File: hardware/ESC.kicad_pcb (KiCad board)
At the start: 2 copper layers, 60 x 25 mm, 83 parts, among them J1 +, J2 -, J3 Conn_01x03, J4 +, J5 +, J6 +, J7 Conn_01x03, Q1 AGM60P30AP, Q2 AGM60P30AP, Q3 AGM60P30AP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

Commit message: layout first draft
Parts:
- C10, C11, C12, C13, C7, C9, D2, FB1, R10, R13, R14, R15: moved to B.Cu
- C14: footprint Capacitor_SMD:C_0402_1005Metric -> Capacitor_SMD:C_0603_1608Metric; moved to B.Cu
- C22, C23: footprint Capacitor_SMD:C_0603_1608Metric -> Capacitor_SMD:C_0402_1005Metric
- C29, C8: footprint Capacitor_SMD:C_0402_1005Metric -> Capacitor_SMD:C_0603_1608Metric
- Q7: value NCE55P30K -> AGM60P30A; footprint Package_TO_SOT_SMD:TO-252-2 -> Package_DFN_QFN:PQFN-8-EP_6x5mm_P1.27mm_Generic; moved to B.Cu
- moved C6 83.0 mm to (180.3, 104.9), turned to 90 degrees
- moved C2 82.8 mm to (180.3, 88.7), turned to 90 degrees
- moved C4 82.8 mm to (180.3, 96.6), turned to 90 degrees
- moved C5 79.3 mm to (176.0, 108.2), turned to -90 degrees
- moved C3 78.8 mm to (176.0, 99.9), turned to -90 degrees
- moved C1 78.6 mm to (176.0, 92.0), turned to -90 degrees
- moved C25 76.2 mm to (178.7, 107.1), turned to 90 degrees
- moved C17 76.1 mm to (178.4, 104.4), turned to 180 degrees
- moved C22 75.4 mm to (178.8, 98.8), turned to 90 degrees
- moved C16 75.4 mm to (178.4, 96.1), turned to 180 degrees
- moved C15 75.2 mm to (178.4, 88.2), turned to 180 degrees
- moved R9 73.9 mm to (181.5, 105.5), turned to 90 degrees
- moved R2 73.6 mm to (181.5, 89.3), turned to 90 degrees
- moved R6 72.9 mm to (181.5, 97.2), turned to 90 degrees
- moved R16 72.7 mm to (181.3, 99.2), turned to 180 degrees
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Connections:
- C3 pad 2: /MOTOR_A -> /MOTOR_B
- C5 pad 2: /MOTOR_A -> /MOTOR_C
- J5 pad 1: /MOTOR_A -> /MOTOR_B
- J6 pad 1: /MOTOR_A -> /MOTOR_C
- Q3 pad 1: /MOTOR_A -> /MOTOR_B
- Q3 pad 2: /GHA -> /GHB
- Q4 pad 2: /GLA -> /GLB
- Q4 pad 3: /MOTOR_A -> /MOTOR_B
- Q5 pad 1: /MOTOR_A -> /MOTOR_C
- Q5 pad 2: /GHA -> /GHC
- Q6 pad 2: /GLA -> /GLC
- Q6 pad 3: /MOTOR_A -> /MOTOR_C
- Q7 pad 1: (no net) -> VBUS
- Q7 pad 2: (no net) -> Net-(Q7-G)
- Q7 pad 3: (no net) -> Net-(D2-A2)
- R13 pad 1: Net-(Q7-PadG) -> Net-(Q7-G)
- R16 pad 1: /MOTOR_A -> /MOTOR_B
- R22 pad 1: /MOTOR_A -> /MOTOR_C
- R6 pad 1: /MOTOR_A -> /MOTOR_B
- R9 pad 1: /MOTOR_A -> /MOTOR_C
- U1 pad 16: /SHB -> /MOTOR_B
- U1 pad 19: /SHC -> /MOTOR_C
- U1 pad 49: unconnected-(U1-EP-Pad49) -> GND
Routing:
- net GND: track 0.00 -> 23.5 mm, vias 0 -> 50
- net /BGND: track 0.00 -> 5.17 mm
- net Net-(U1-CB): track 0.00 -> 1.32 mm
- net VBUS: track 0.00 -> 1.24 mm, vias 0 -> 100
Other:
- copper layers 2 -> 4

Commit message: started routing schematic
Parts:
- added J8: +, Connector_Wire:SolderWirePad_1x01_SMD_2x4mm, B.Cu at (151.6, 107.0)
- added J9: +, Connector_Wire:SolderWirePad_1x01_SMD_2x4mm, B.Cu at (155.1, 107.0)
- J3: value Conn_01x03 -> +; footprint Connector_PinHeader_2.54mm:PinHeader_1x03_P2.54mm_Vertical -> Connector_Wire:SolderWirePad_1x01_SMD_2x4mm; moved to B.Cu
- moved J3 8.47 mm to (148.0, 107.0), turned to 0 degrees
- moved J1 8.00 mm to (142.0, 89.0)
- moved J2 8.00 mm to (142.0, 106.0)
- moved J7 8.00 mm to (140.0, 95.0)
- moved JP1 7.95 mm to (143.1, 98.2)
- moved R20 7.95 mm to (143.3, 100.3)
- moved D2 7.30 mm to (148.6, 88.1)
- moved Q7 7.20 mm to (148.8, 92.8)
- moved R13 7.20 mm to (150.9, 96.5)
- moved C32 7.20 mm to (146.4, 94.2)
- moved R24 7.20 mm to (148.4, 94.2)
- moved R25 7.20 mm to (147.4, 94.2)
- moved C18 7.15 mm to (166.2, 89.7)
- moved C19 7.15 mm to (158.2, 89.6)
- moved C20 7.15 mm to (150.0, 89.6)
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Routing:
- net /MOTOR_A: track 0.00 -> 55.4 mm, vias 0 -> 1
- net /SPA: track 0.00 -> 42.3 mm, vias 0 -> 2
- net /GLA: track 0.00 -> 38.2 mm, vias 0 -> 2
- net VBUS: track 1.24 -> 26.4 mm, vias 100 -> 64
- net /GHA: track 0.00 -> 22.3 mm, vias 0 -> 2
- net /MOTOR_C: track 0.00 -> 12.5 mm
- net /MOTOR_B: track 0.00 -> 12.5 mm
- net /VIRTUAL_N: track 0.00 -> 9.69 mm
- net /SPC: track 0.00 -> 8.08 mm, vias 0 -> 1
- net /SPB: track 0.00 -> 7.92 mm, vias 0 -> 1
- net /HSE_IN: track 0.00 -> 6.72 mm
- net /BEMF_C: track 0.00 -> 5.02 mm
- net +3.3V: track 0.00 -> 4.88 mm
- net /BEMF_B: track 0.00 -> 4.81 mm
- net /BEMF_A: track 0.00 -> 4.59 mm
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- added copper zone on B.Cu, net /MOTOR_A
- added copper zone on B.Cu, net /MOTOR_B
- added copper zone on B.Cu, net /MOTOR_C
- added copper zone on B.Cu, net Net-(D2-A2)
- added copper zone on B.Cu, net VBUS
- added copper zone on F.Cu, net VBUS
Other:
- board size 60 x 25 mm -> 52 x 25 mm

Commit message: routing pcb
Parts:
- JP1, R11, R12, R20: moved to B.Cu
- moved C14 15.0 mm to (155.1, 98.3), turned to 180 degrees
- moved R11 13.6 mm to (161.0, 94.7), turned to 90 degrees
- moved R12 13.6 mm to (162.0, 94.7), turned to -90 degrees
- moved R10 12.9 mm to (157.1, 98.2), turned to -90 degrees
- moved C9 12.0 mm to (156.5, 99.5), turned to 180 degrees
- moved FB1 11.8 mm to (164.7, 107.5), turned to -90 degrees
- moved C11 11.7 mm to (159.3, 97.1), turned to 180 degrees
- moved C12 11.4 mm to (160.8, 96.9), turned to 90 degrees
- moved C10 11.2 mm to (161.7, 96.9), turned to 90 degrees
- moved C13 11.2 mm to (157.6, 106.2), turned to 180 degrees
- moved C7 9.95 mm to (157.1, 101.0), turned to 90 degrees
- moved R14 9.70 mm to (163.5, 107.0), turned to -90 degrees
- moved R15 9.17 mm to (162.5, 107.0), turned to -90 degrees
- moved C8 4.22 mm to (167.2, 95.5), turned to 180 degrees
- moved C32 2.02 mm to (144.5, 93.5)
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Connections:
- U1 pad 31: /SCLK -> /SCK
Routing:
- net /MOTOR_A: track 55.4 -> 31.2 mm, vias 1 -> 0
- net /GLB: track 0.00 -> 19.3 mm, vias 0 -> 2
- net /SPA: track 42.3 -> 23.6 mm, vias 2 -> 4
- net /GLC: track 0.00 -> 18.6 mm, vias 0 -> 2
- net /SOA: track 0.00 -> 18.3 mm, vias 0 -> 2
- net /DIR: track 0.00 -> 17.4 mm, vias 0 -> 1
- net /PWM_IN: track 0.00 -> 17.1 mm
- net /SOC: track 0.00 -> 16.9 mm, vias 0 -> 2
- net /SOB: track 0.00 -> 16.7 mm, vias 0 -> 2
- net /NSS: track 0.00 -> 16.7 mm, vias 0 -> 1
- net /SCK: track 0.00 -> 14.6 mm, vias 0 -> 1
- net /MISO: track 1.13 -> 14.5 mm, vias 0 -> 1
- net /IN_ADC: track 3.27 -> 16.3 mm, vias 1 -> 2
- net /GLA: track 38.2 -> 25.4 mm
- net /MOSI: track 0.00 -> 12.6 mm, vias 0 -> 1
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- added copper zone on B.Cu, net /SPA
- added copper zone on F.Cu, net /SPA
- added copper zone on B.Cu, net /SPB
- added copper zone on F.Cu, net /SPB
- added copper zone on B.Cu, net /SPC
- added copper zone on F.Cu, net /SPC

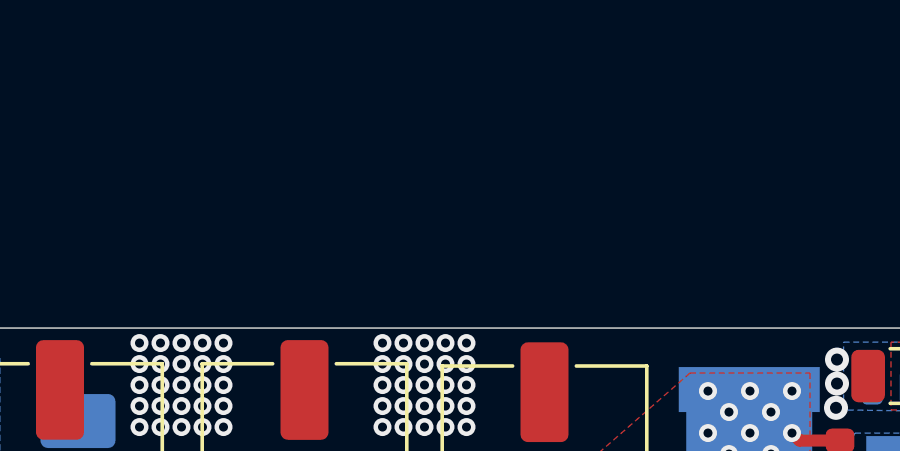
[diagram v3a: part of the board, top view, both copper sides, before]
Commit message: updated to kicad 10.0
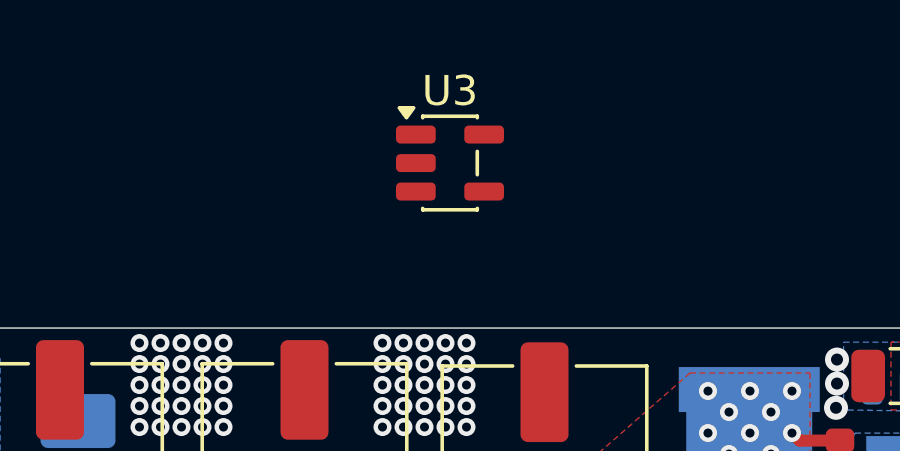
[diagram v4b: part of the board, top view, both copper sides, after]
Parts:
- added U3: LMV321, Package_TO_SOT_SMD:SOT-23-5, F.Cu at (163.0, 79.5)

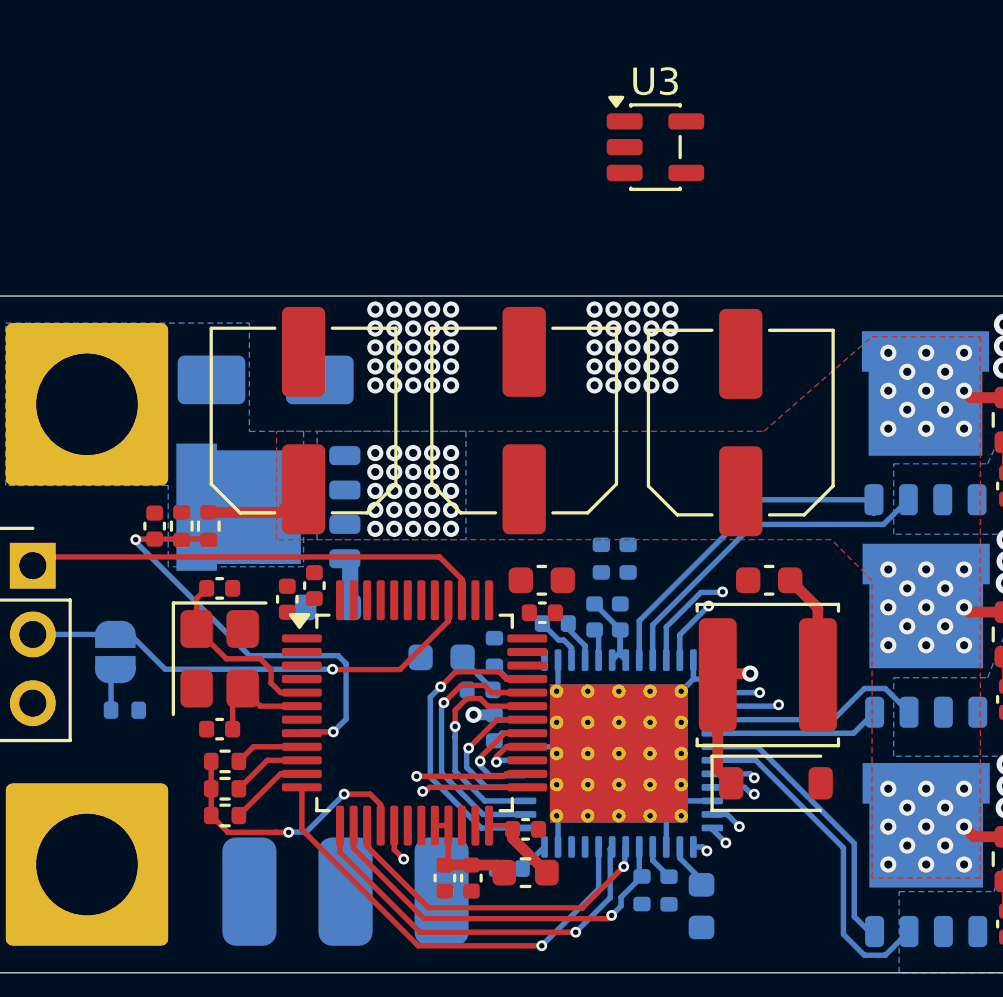
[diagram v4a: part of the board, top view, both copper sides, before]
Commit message: moved regulator
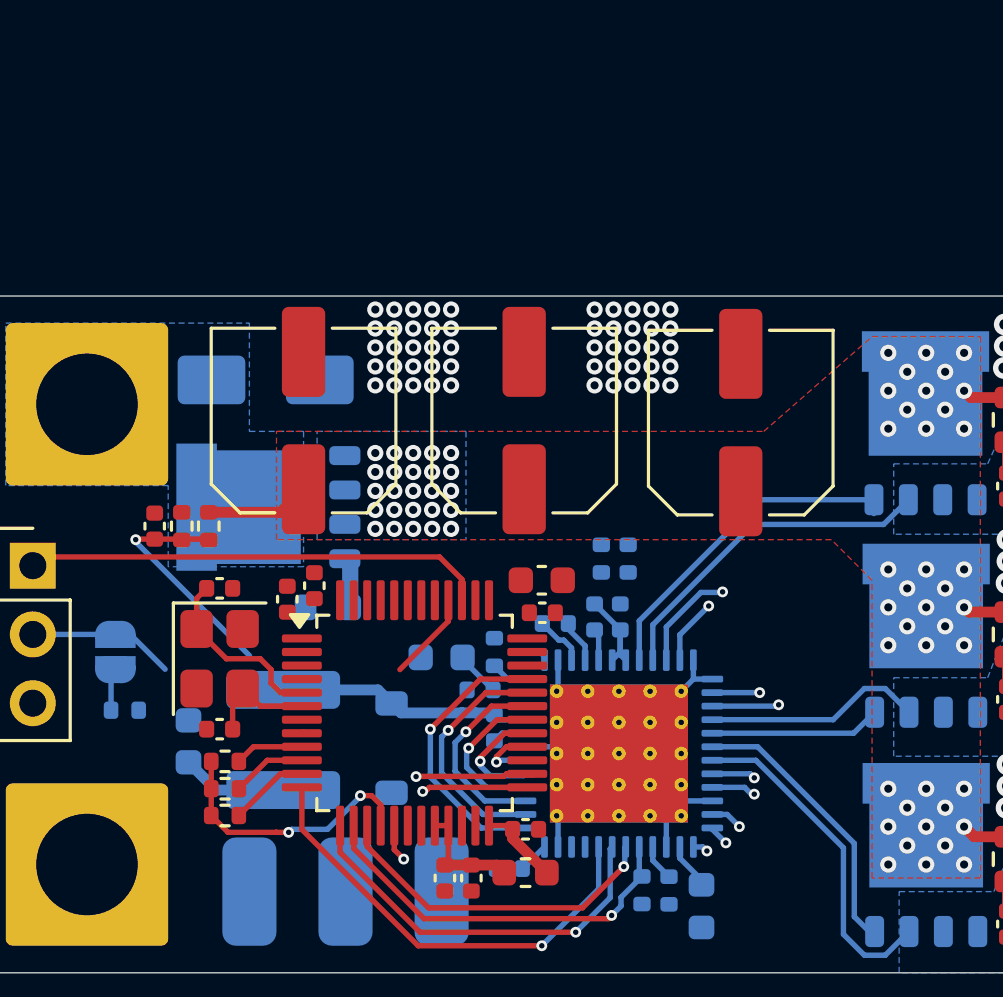
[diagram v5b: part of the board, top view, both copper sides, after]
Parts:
- removed U3: LMV321, Package_TO_SOT_SMD:SOT-23-5
- C8, D1, L1: moved to B.Cu
- moved C8 22.3 mm to (145.8, 101.5), turned to 90 degrees
- moved L1 18.1 mm to (149.2, 101.4), turned to -90 degrees
- moved D1 14.3 mm to (153.2, 101.7), turned to -90 degrees
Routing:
- net /BGND: track 18.3 -> 9.41 mm, vias 2 -> 0
- net /DIR: track 17.4 -> 8.72 mm, vias 1 -> 0
- net /IN_ADC: track 16.3 -> 8.78 mm, vias 2 -> 1
- net /INHB: track 8.27 -> 7.34 mm
- net /INLA: track 9.82 -> 8.91 mm
- net /INHA: track 11.3 -> 10.4 mm

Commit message: finished pcb
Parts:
- moved R12 4.31 mm to (157.8, 95.7), turned to 0 degrees
- moved R11 3.77 mm to (157.8, 96.7), turned to 180 degrees
- moved R19 0.91 mm to (179.9, 91.8)
- moved R23 0.91 mm to (179.8, 108.0)
- moved C25 0.91 mm to (178.8, 108.0)
- moved C23 0.90 mm to (178.9, 91.8)
- moved C22 0.88 mm to (178.9, 99.7)
- moved R17 0.88 mm to (179.9, 99.7)
- moved FB1 0.65 mm to (165.3, 107.8)
- moved R14 0.65 mm to (164.1, 107.2)
- moved R15 0.65 mm to (163.1, 107.2)
- moved C11 0.42 mm to (159.7, 97.1)
- moved C10 0.40 mm to (162.1, 96.9)
- moved C12 0.40 mm to (161.2, 96.9)
- moved C13 0.40 mm to (158.0, 106.2)
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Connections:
- U2 pad 44: unconnected-(U2-PB7-Pad44) -> /DRV_CAL
- U2 pad 46: unconnected-(U2-PB9-Pad46) -> /DRV_EN
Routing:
- net +3.3V: track 6.98 -> 46.9 mm, vias 0 -> 5
- net /BEMF_A: track 4.59 -> 42.7 mm, vias 0 -> 2
- net /BEMF_B: track 4.81 -> 41.5 mm, vias 0 -> 2
- net /BEMF_C: track 5.02 -> 38.4 mm, vias 0 -> 2
- net /DRV_EN: track 0.00 -> 25.4 mm, vias 0 -> 2
- net /DRV_CAL: track 0.00 -> 23.7 mm, vias 0 -> 2
- net GND: track 17.5 -> 36.5 mm, vias 59 -> 78
- net /SWDIO: track 0.00 -> 17.3 mm, vias 0 -> 2
- net /SWCLK: track 0.00 -> 14.5 mm, vias 0 -> 2
- net VBUS: track 15.5 -> 29.3 mm
- net /IN_ADC: track 8.78 -> 17.0 mm, vias 1 -> 2
- net /DIR: track 8.72 -> 16.9 mm, vias 0 -> 1
- net /MOTOR_B: track 20.6 -> 15.0 mm, vias 0 -> 1
- net /MOTOR_A: track 31.2 -> 25.8 mm, vias 0 -> 1
- net /MOTOR_C: track 25.0 -> 19.8 mm, vias 0 -> 1
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- added copper zone on In2.Cu, net +3.3V
- added copper zone on B.Cu, net GND
- added copper zone on F.Cu, net GND
- added copper zone on In1.Cu, net GND
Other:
- board text added: "CCW"
- board text added: "CW"
- board text added: "V1.0"

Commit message: added boot button and reset pad
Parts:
- added J10: +, Connector_Wire:SolderWirePad_1x01_SMD_2x4mm, B.Cu at (167.0, 88.0)
- added R28: 10K, Resistor_SMD:R_0402_1005Metric, F.Cu at (163.6, 97.4)
- added SW3: SW_Push, Button_Switch_SMD:SW_Push_SPST_NO_Alps_SKRK, F.Cu at (166.9, 97.4)
- moved R15 0.21 mm to (163.1, 107.4)
- moved R14 0.21 mm to (164.1, 107.4)
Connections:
- U2 pad 43: unconnected-(U2-PB6-Pad43) -> /FAULT
- U2 pad 45: unconnected-(U2-PB8-Pad45) -> /BOOT
- U2 pad 7: unconnected-(U2-PG10-Pad7) -> /RESET
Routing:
- net /RESET: track 0.00 -> 26.7 mm, vias 0 -> 2
- net /FAULT: track 1.67 -> 23.5 mm, vias 0 -> 2
- net /BOOT: track 0.00 -> 16.0 mm, vias 0 -> 2
- net GND: track 36.5 -> 46.6 mm, vias 78 -> 74
- net +3.3V: track 46.9 -> 51.7 mm, vias 5 -> 6
- net /PWM_IN: track 17.1 -> 17.9 mm
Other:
- board text added: "BOOT"
- board text added: "GND"
- board text added: "RST"
- board text added: "SWCLK"
- board text added: "SWDIO"

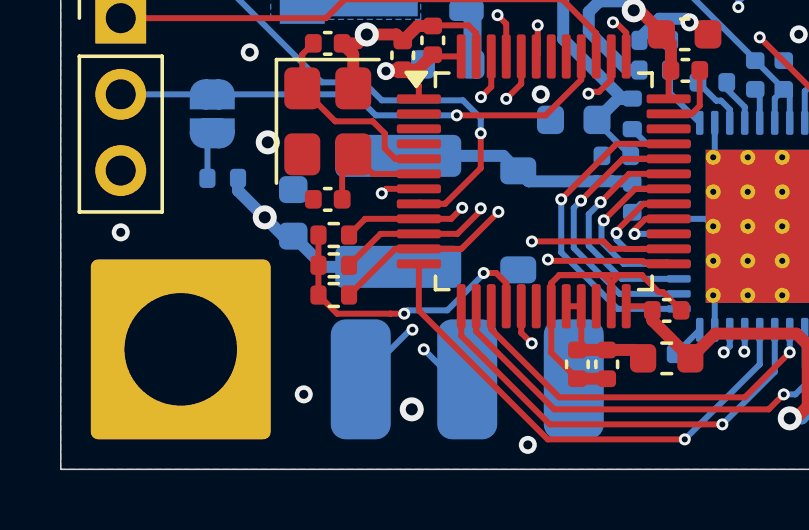
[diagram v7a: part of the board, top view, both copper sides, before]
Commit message: added filter cap to virtual gnd
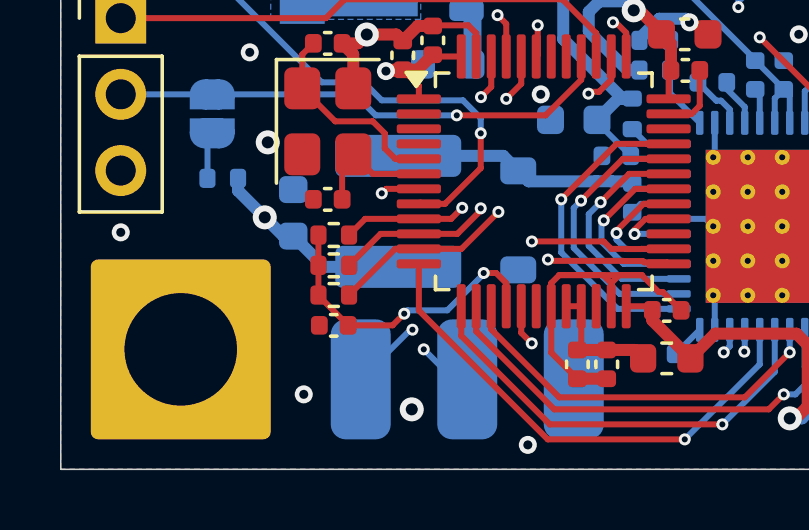
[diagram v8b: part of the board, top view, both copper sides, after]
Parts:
- added C34: 1nF, Capacitor_SMD:C_0402_1005Metric, F.Cu at (147.1, 105.2)
